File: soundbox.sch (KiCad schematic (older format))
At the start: 180 parts, among them J10 COLOR INPUT, J11 MONO INPUT, J12 NEXT PWR INPUT 1, J13 NEXT PWR INPUT 2, J14 -12VDC OUT, J15 5VDC STANDBY, J16 MON IN 1, J17 MON IN 2, J18 PA1, J19 BOOT0, J2 OUT (SJ1-3535NG), J20 PC0, J21 PC1, J22 PB0, J23 PB1, J24 R SPK, J25 R SPEAKER (SJ-2509N), J26 L SPEAKER, J27 L SPK, J28 I2C Ext, J29 OLED, J3 MIC (SJ1-3535NG), J31 NeXT Keyboard, J32 NeXT Keyboard (MD-50SM / KMDG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, J4 USB Host (SS-52100-001), J5 Mic IN, J6 Audio OUT, J7 STLINK, J8 UART2, J9 PA0, Q1 2SC2712, SW1 NeXT POWER SW (1-1825027-1 / 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, SW3 NeXT POWER SW, SW4 MCU RESET, U11 TLV70033DDCR, U17 USBLC6-2SC6, U18 STMPS2141STR, U19 SN74LVC2G34DBV, U20 PCM5122PW, U21 TLV70033DDCR (or XC6204B332MR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, U22 TLV70033DDCR (or XC6204B332MR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, U23 PLT133/T, U24 STM32F401RCT6, U25 SN74LVC1G07DBV, U26 SN74HCT125DR, U27 TLV320ADC3100, U28 BD33FC0FP, U29 TPA2005D1DGN, U30 BD33FC0FP, U31 TPA2005D1DGN, U32 PCA9515D, U8 5V(DC/DC), X3 ECS-2520MVLC-225.792-BN-TR, Y2 25MHz (FA-238 25.0000MB-K0)

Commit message: update position
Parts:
- U18: value STMPS2141STR -> STMPS2151STR‎ or TPS2051CDBV
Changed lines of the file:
@@
 P 13850 6550
 F 0 "U18" H 14344 6828 60  0000 L CNN
-F 1 "STMPS2141STR" H 14344 6722 60  0000 L CNN
+F 1 "STMPS2151STR‎ or TPS2051CDBV" H 14344 6722 60  0000 L CNN
 F 2 "Package_TO_SOT_SMD:SOT-23-5_HandSoldering" H 13850 6550 60  0001 C CNN
 F 3 "" H 13850 6550 60  0001 C CNN

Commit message: update PCB
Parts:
- added JP6: Use Dummy Load, Connector_PinHeader_2.54mm:PinHeader_1x02_P2.54mm_Vertical, symbol Connector_Generic:Conn_01x02
- R31: value 2x 120 5W (or 56ohm 7W) -> 2x 100 5W (or 47ohm 7W)
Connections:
- net GND: now also JP6.1 (Pin_1); no longer R31.2
- new net: JP6.2 (Pin_2), R31.2
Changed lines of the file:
@@
 P 2700 2250
 F 0 "R31" H 2770 2296 50  0000 L CNN
-F 1 "2x 120 5W (or 56ohm 7W)" H 2770 2205 50  0000 L CNN
+F 1 "2x 100 5W (or 47ohm 7W)" H 2770 2205 50  0000 L CNN
 F 2 "Resistor_THT:R_Axial_DIN0617_L17.0mm_D6.0mm_P30.48mm_Horizontal" V 2630 2250 50  0001 C CNN
 F 3 "~" H 2700 2250 50  0001 C CNN
@@
 L ossc_board-rescue:GND-RESCUE-ossc_board #PWR059
 U 1 1 5FBC0130
-P 2700 2500
-F 0 "#PWR059" H 2700 2500 30  0001 C CNN
-F 1 "GND-RESCUE-ossc_board" H 2700 2430 30  0001 C CNN
-F 2 "" H 2700 2500 60  0000 C CNN
-F 3 "" H 2700 2500 60  0000 C CNN
-	1    2700 2500
-	1    0    0    -1
+P 2300 2650
+F 0 "#PWR059" H 2300 2650 30  0001 C CNN
+F 1 "GND-RESCUE-ossc_board" H 2300 2580 30  0001 C CNN
+F 2 "" H 2300 2650 60  0000 C CNN
+F 3 "" H 2300 2650 60  0000 C CNN
+	1    2300 2650
+	0    -1   -1   0
 $EndComp
 Wire Wire Line
-	2700 2400 2700 2500
-Wire Wire Line
 	2700 2100 2700 2000
 Wire Wire Line
@@
 	1    0    0    -1
 $EndComp
+$Comp
+L Connector_Generic:Conn_01x02 JP6
+U 1 1 5F626198
+P 2100 2650
+F 0 "JP6" H 2180 2642 50  0000 L CNN
+F 1 "Use Dummy Load" H 2180 2551 50  0000 L CNN
+F 2 "Connector_PinHeader_2.54mm:PinHeader_1x02_P2.54mm_Vertical" H 2100 2650 50  0001 C CNN
+F 3 "~" H 2100 2650 50  0001 C CNN
+	1    2100 2650
+	-1   0    0    1
+$EndComp
+Wire Wire Line
+	2700 2400 2700 2550
+Wire Wire Line
+	2300 2550 2700 2550
 $EndSCHEMATC

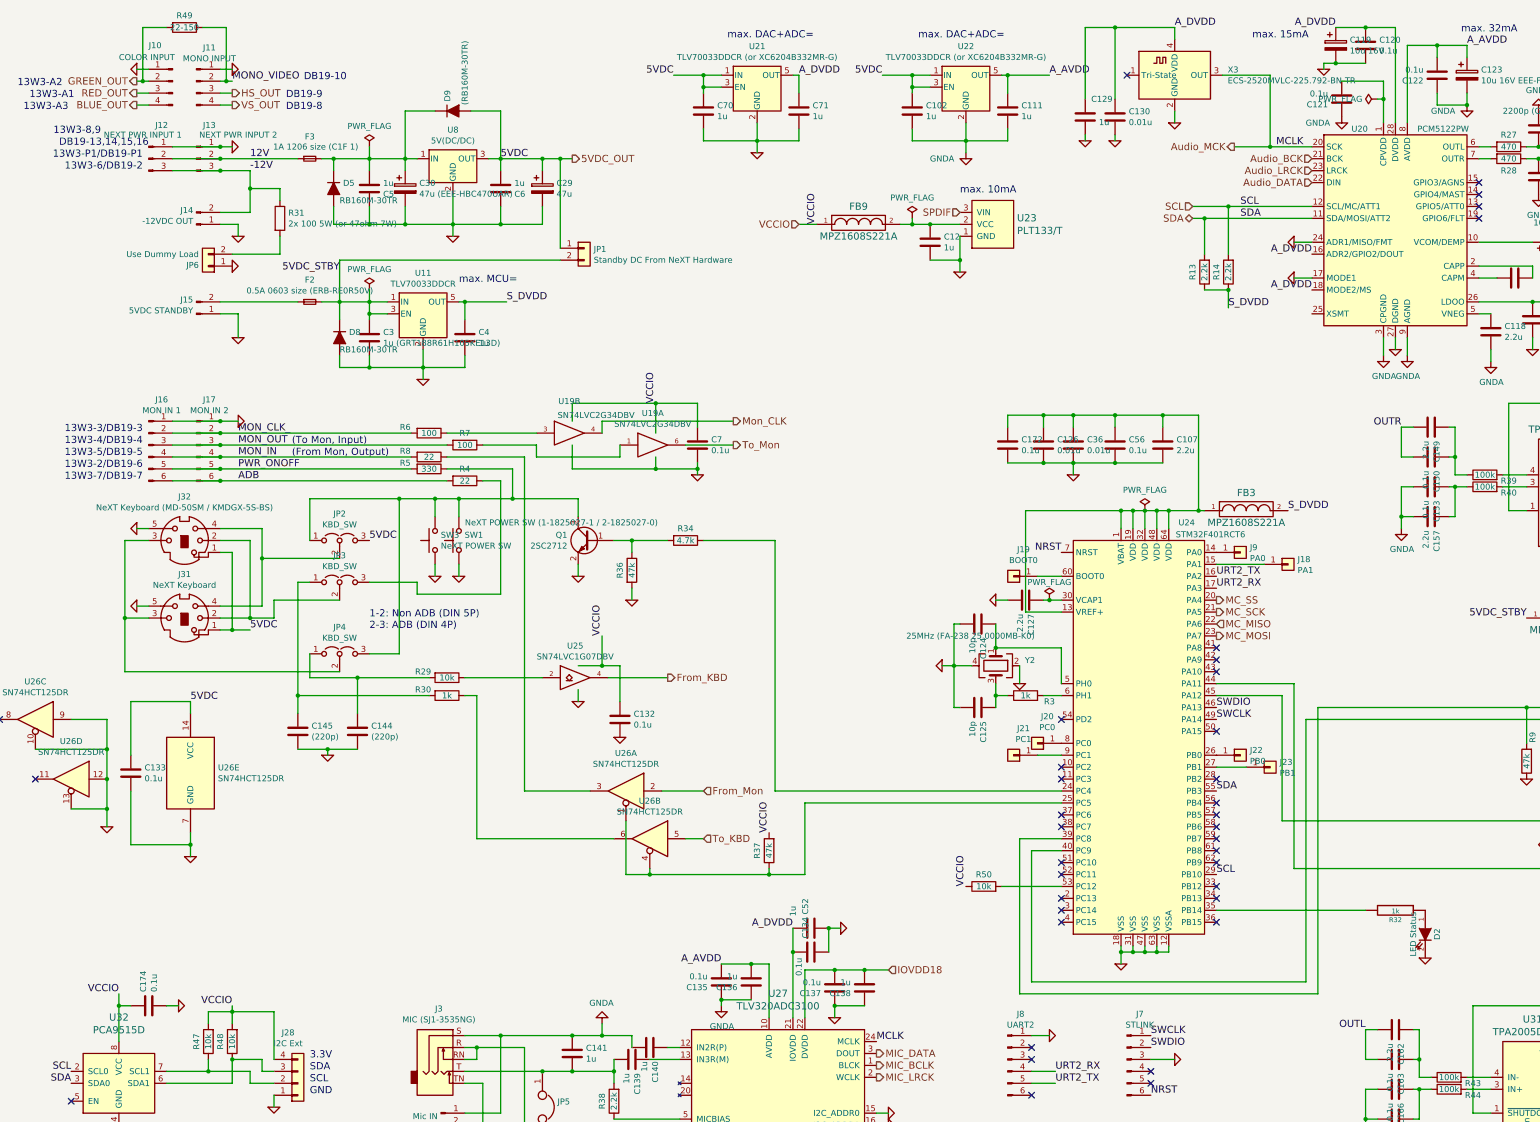
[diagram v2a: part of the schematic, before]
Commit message: fix wrong connection
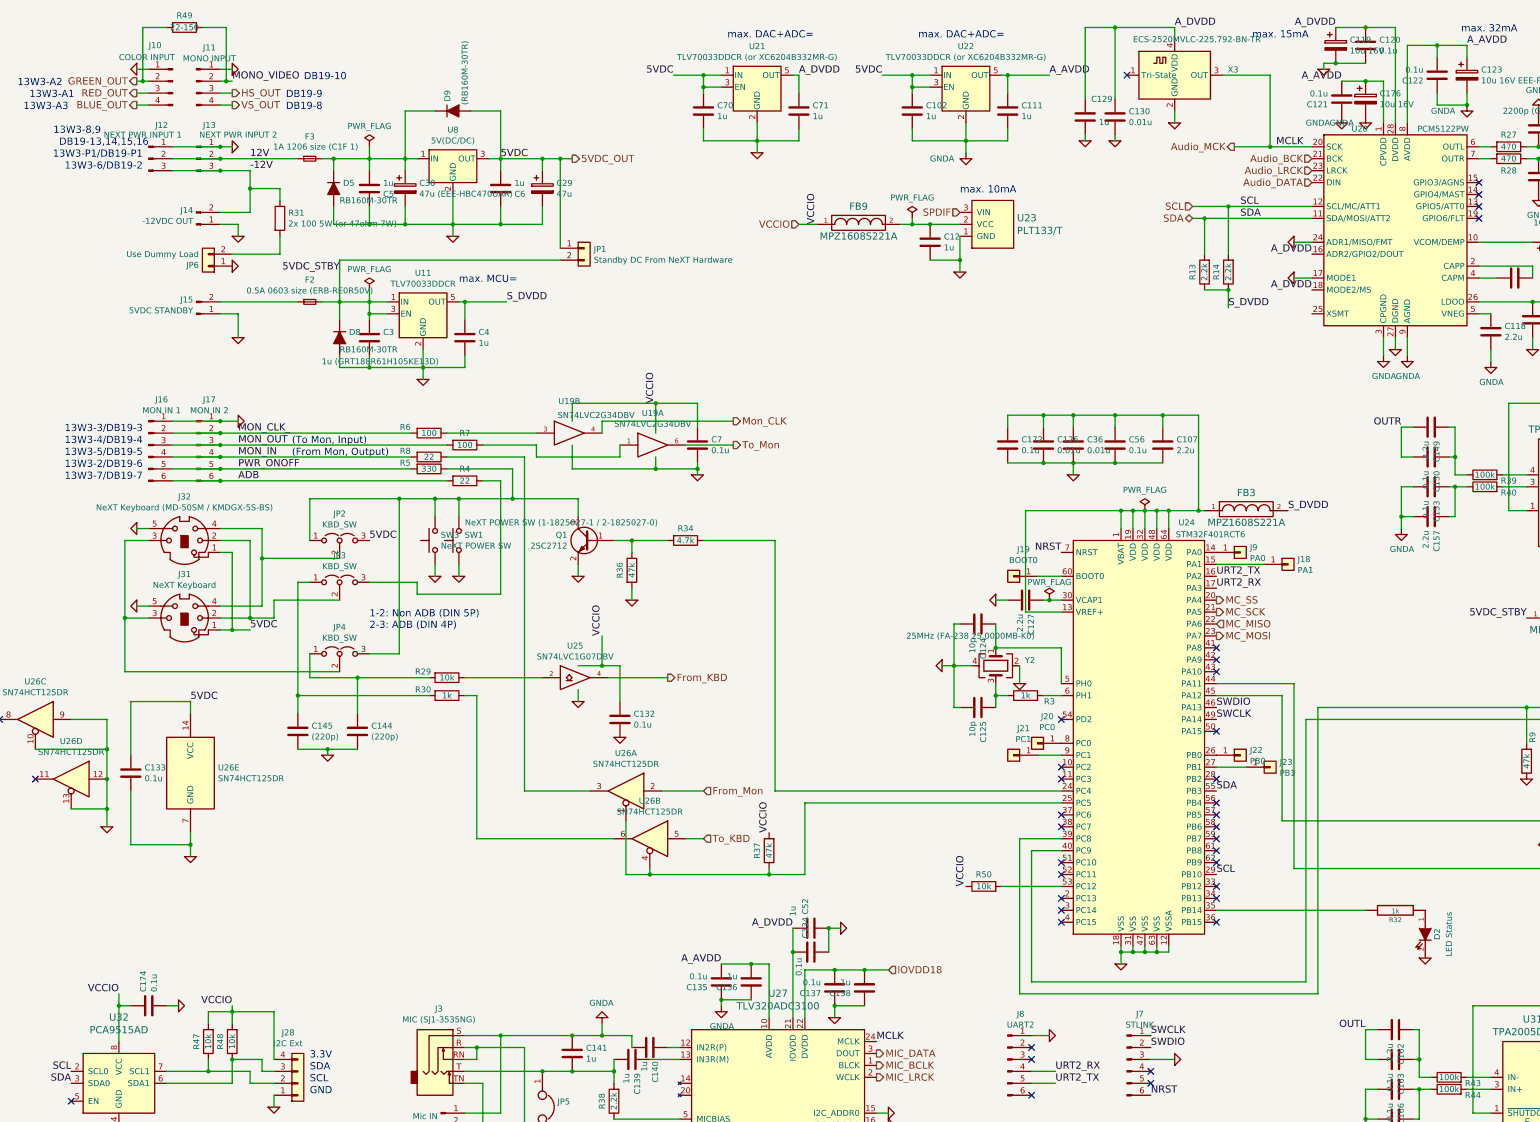
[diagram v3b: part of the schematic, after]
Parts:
- added C176: 10u 16V, Capacitor_SMD:CP_Elec_4x4.5, symbol Device:CP
- U32: value PCA9515D -> PCA9515AD
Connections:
- net A_AVDD: now also C121.2, U20.1 (CPVDD), C176.1
- net GNDA: now also C176.2
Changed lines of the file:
@@
 P 3450 3250
 F 0 "C3" H 3565 3296 50  0000 L CNN
-F 1 "1u (GRT188R61H105KE13D)" H 3565 3205 50  0000 L CNN
+F 1 "1u (GRT188R61H105KE13D)" H 3050 3050 50  0000 L CNN
 F 2 "Capacitor_SMD:C_0603_1608Metric_Pad1.05x0.95mm_HandSolder" H 3488 3100 50  0001 C CNN
 F 3 "~" H 3450 3250 50  0001 C CNN
@@
 $EndComp
 Wire Wire Line
-	11950 1450 11950 1250
-Wire Wire Line
-	11950 1100 11600 1100
+	11950 1100 11800 1100
 $Comp
 L Device:C C120
@@
 AR Path="/5F595115/5FCBC1B3" Ref="D2"  Part="1"
 F 0 "D2" H 12300 8350 50  0000 C CNN
-F 1 "LED Status" H 12300 8150 50  0000 C CNN
+F 1 "LED Status" H 12300 8450 50  0000 C CNN
 F 2 "LED_THT:LED_D3.0mm_Horizontal_O1.27mm_Z6.0mm" H 12300 8250 60  0001 C CNN
 F 3 "~" H 12300 8250 60  0000 C CNN
@@
 P 10200 1050
 F 0 "X3" H 10644 1096 50  0000 L CNN
-F 1 "ECS-2520MVLC-225.792-BN-TR" H 10644 1005 50  0000 L CNN
+F 1 "ECS-2520MVLC-225.792-BN-TR" H 9850 1350 50  0000 L CNN
 F 2 "Oscillator:Oscillator_SMD_SeikoEpson_SG210-4Pin_2.5x2.0mm_HandSoldering" H 10650 700 50  0001 C CNN
 F 3 "https://www.ecsxtal.com/store/pdf/ECS-2520MV.pdf" H 10025 1175 50  0001 C CNN
@@
 	3450 2850 3450 2950
 $Comp
-L power:PWR_FLAG #FLG0106
-U 1 1 6245E5AE
-P 11900 1250
-F 0 "#FLG0106" H 11900 1325 50  0001 C CNN
-F 1 "PWR_FLAG" V 11900 1377 50  0000 L CNN
-F 2 "" H 11900 1250 50  0001 C CNN
-F 3 "~" H 11900 1250 50  0001 C CNN
-	1    11900 1250
-	0    -1   -1   0
-$EndComp
-Wire Wire Line
-	11900 1250 11950 1250
-Connection ~ 11950 1250
-Wire Wire Line
-	11950 1250 11950 1100
-$Comp
 L power:PWR_FLAG #FLG0107
 U 1 1 6249EA31
@@
 P 1350 9750
 F 0 "U32" H 1350 10553 60  0000 C CNN
-F 1 "PCA9515D" H 1350 10447 60  0000 C CNN
+F 1 "PCA9515AD" H 1350 10447 60  0000 C CNN
 F 2 "Package_SO:SOIC-8_3.9x4.9mm_P1.27mm" H 1350 9750 60  0001 C CNN
 F 3 "" H 1350 9750 60  0001 C CNN
@@
 Wire Wire Line
 	2300 2550 2700 2550
+Wire Wire Line
+	11950 1100 11950 1450
+$Comp
+L Device:CP C176
+U 1 1 5F8ECE8C
+P 11800 1250
+F 0 "C176" H 11918 1296 50  0000 L CNN
+F 1 "10u 16V" H 11918 1205 50  0000 L CNN
+F 2 "Capacitor_SMD:CP_Elec_4x4.5" H 11838 1100 50  0001 C CNN
+F 3 "~" H 11800 1250 50  0001 C CNN
+	1    11800 1250
+	1    0    0    -1
+$EndComp
+Connection ~ 11800 1100
+Wire Wire Line
+	11800 1100 11600 1100
+$Comp
+L power:GNDA #PWR0272
+U 1 1 5F8EE664
+P 11800 1400
+F 0 "#PWR0272" H 11800 1150 50  0001 C CNN
+F 1 "GNDA" H 11600 1350 50  0000 C CNN
+F 2 "" H 11800 1400 50  0001 C CNN
+F 3 "" H 11800 1400 50  0001 C CNN
+	1    11800 1400
+	1    0    0    -1
+$EndComp
+Text Label 11600 1100 2    60   ~ 0
+A_AVDD
 $EndSCHEMATC

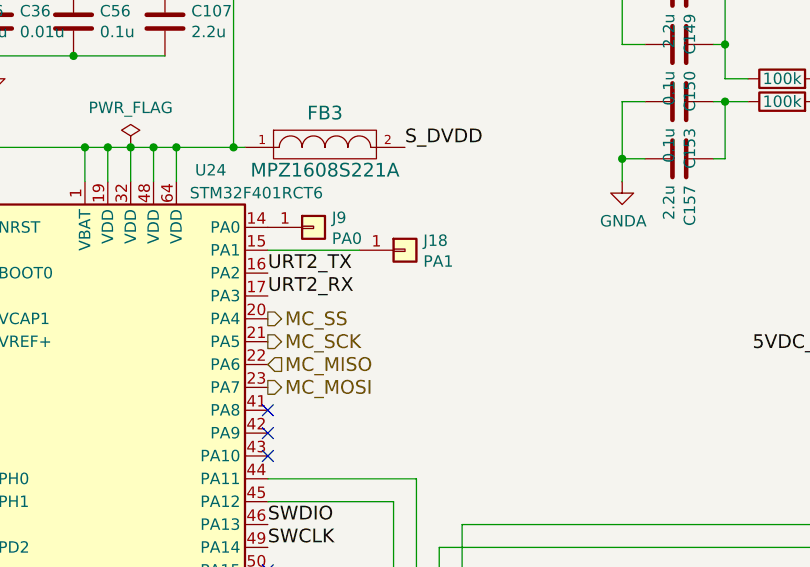
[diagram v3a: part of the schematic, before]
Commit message: add uart registors
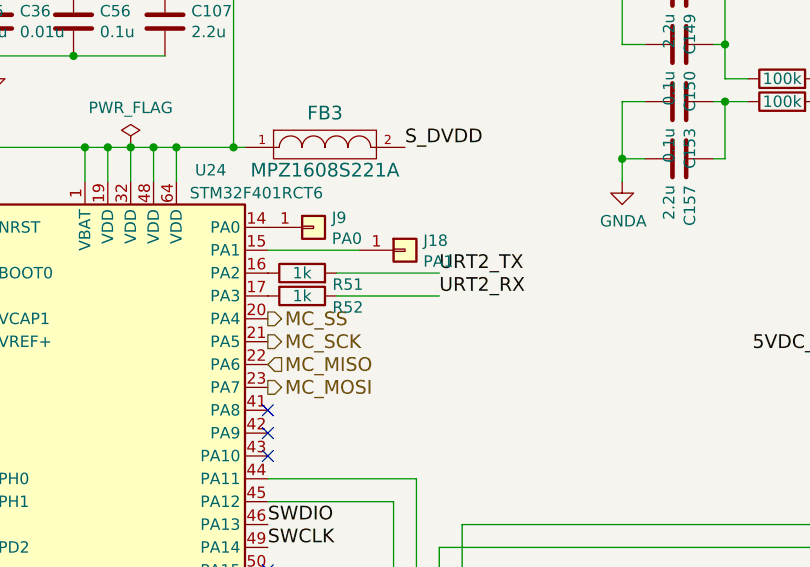
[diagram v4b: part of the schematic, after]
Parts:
- added R51, R52: 1k, Resistor_SMD:R_0603_1608Metric_Pad1.05x0.95mm_HandSolder, symbol Device:R
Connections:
- net URT2_RX: now also R52.2; no longer U24.17 (PA3)
- net URT2_TX: now also R51.2; no longer U24.16 (PA2)
- new net: R51.1, U24.16 (PA2)
- new net: R52.1, U24.17 (PA3)
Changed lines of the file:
@@
 Wire Wire Line
 	9000 9400 9200 9400
-Text Label 10550 5250 0    60   ~ 0
+Text Label 11300 5250 0    60   ~ 0
 URT2_TX
-Text Label 10550 5350 0    60   ~ 0
+Text Label 11300 5350 0    60   ~ 0
 URT2_RX
 NoConn ~ 9000 9200
@@
 Text Label 11600 1100 2    60   ~ 0
 A_AVDD
+$Comp
+L Device:R R51
+U 1 1 5F69A64A
+P 10700 5250
+F 0 "R51" V 10650 5050 50  0000 C CNN
+F 1 "1k" V 10700 5250 50  0000 C CNN
+F 2 "Resistor_SMD:R_0603_1608Metric_Pad1.05x0.95mm_HandSolder" V 10630 5250 50  0001 C CNN
+F 3 "~" H 10700 5250 50  0001 C CNN
+	1    10700 5250
+	0    -1   -1   0
+$EndComp
+$Comp
+L Device:R R52
+U 1 1 5F69AC4A
+P 10700 5350
+F 0 "R52" V 10650 5150 50  0000 C CNN
+F 1 "1k" V 10700 5350 50  0000 C CNN
+F 2 "Resistor_SMD:R_0603_1608Metric_Pad1.05x0.95mm_HandSolder" V 10630 5350 50  0001 C CNN
+F 3 "~" H 10700 5350 50  0001 C CNN
+	1    10700 5350
+	0    -1   -1   0
+$EndComp
+Wire Wire Line
+	10850 5250 11300 5250
+Wire Wire Line
+	11300 5350 10850 5350
 $EndSCHEMATC

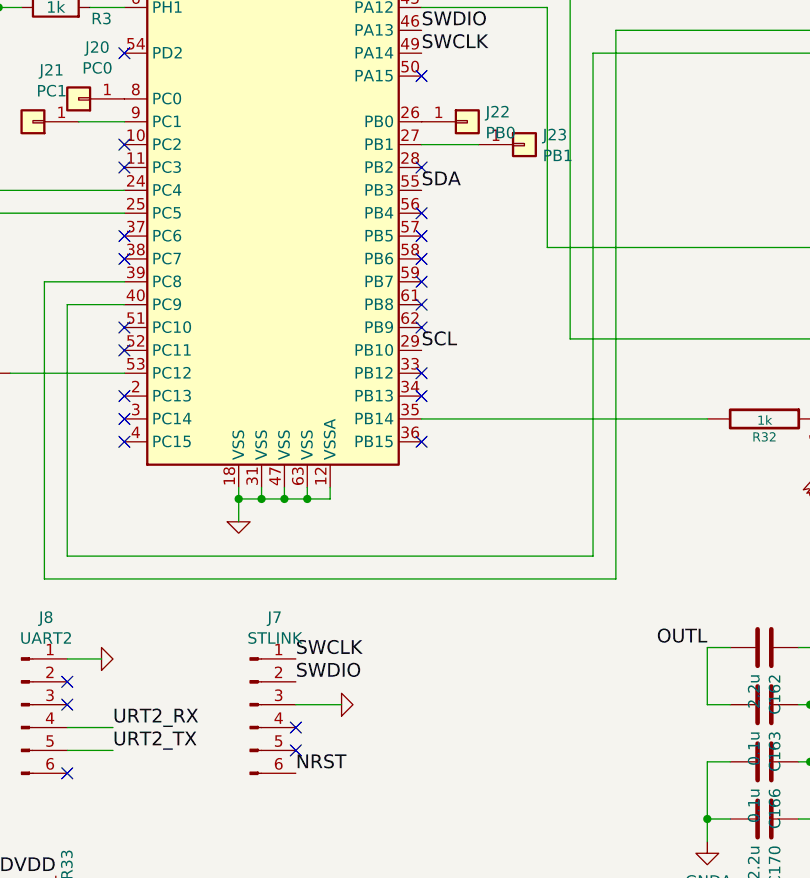
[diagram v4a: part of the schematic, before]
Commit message: add BOOT1 pad
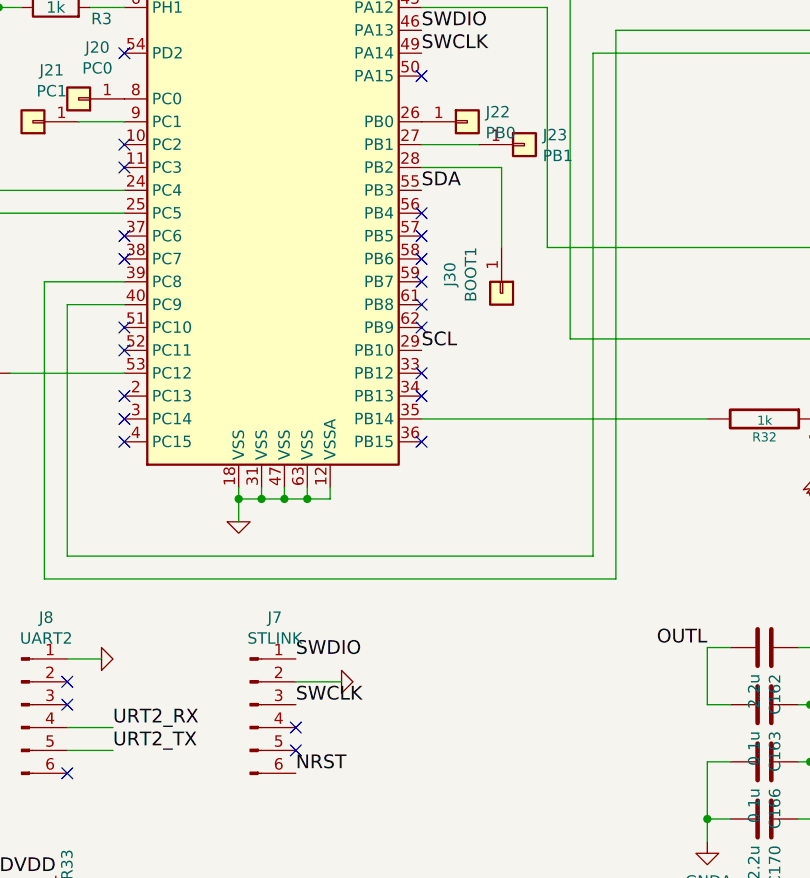
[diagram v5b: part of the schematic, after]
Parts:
- added J30: BOOT1, custom_components:TestPad-D1.0mm, symbol Connector_Generic:Conn_01x01
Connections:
- net GND: now also J7.2 (Pin_2); no longer J7.3 (Pin_3)
- net SWCLK: now also J7.3 (Pin_3); no longer J7.1 (Pin_1)
- net SWDIO: now also J7.1 (Pin_1); no longer J7.2 (Pin_2)
- net at U24.28 (PB2): now also J30.1 (Pin_1)
- no-connect marks 40 -> 39
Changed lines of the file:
@@
 Wire Wire Line
 	8350 6000 8250 6000
+Text Label 10000 9300 0    60   ~ 0
+SWCLK
 Text Label 10000 9100 0    60   ~ 0
-SWCLK
-Text Label 10000 9200 0    60   ~ 0
 SWDIO
 $Comp
 L ossc_board-rescue:GND-RESCUE-ossc_board #PWR069
 U 1 1 5F9B6350
-P 10200 9300
-F 0 "#PWR069" H 10200 9300 30  0001 C CNN
-F 1 "GND-RESCUE-ossc_board" H 10200 9230 30  0001 C CNN
-F 2 "" H 10200 9300 60  0000 C CNN
-F 3 "" H 10200 9300 60  0000 C CNN
-	1    10200 9300
+P 10200 9200
+F 0 "#PWR069" H 10200 9200 30  0001 C CNN
+F 1 "GND-RESCUE-ossc_board" H 10200 9130 30  0001 C CNN
+F 2 "" H 10200 9200 60  0000 C CNN
+F 3 "" H 10200 9200 60  0000 C CNN
+	1    10200 9200
 	0    -1   -1   0
 $EndComp
 Wire Wire Line
-	10200 9300 10000 9300
+	10200 9200 10000 9200
 NoConn ~ 10000 9400
 NoConn ~ 10000 9500
@@
 NoConn ~ 9250 6950
 NoConn ~ 9250 6850
-NoConn ~ 10550 6950
 $Comp
 L power:PWR_FLAG #FLG0102
@@
 Wire Wire Line
 	11300 5350 10850 5350
+$Comp
+L Connector_Generic:Conn_01x01 J30
+U 1 1 5F772179
+P 10900 7500
+F 0 "J30" H 10818 7275 50  0000 C CNN
+F 1 "BOOT1" H 10818 7366 50  0000 C CNN
+F 2 "custom_components:TestPad-D1.0mm" H 10900 7500 50  0001 C CNN
+F 3 "~" H 10900 7500 50  0001 C CNN
+	1    10900 7500
+	0    1    1    0
+$EndComp
+Wire Wire Line
+	10550 6950 10900 6950
+Wire Wire Line
+	10900 6950 10900 7300
 $EndSCHEMATC
